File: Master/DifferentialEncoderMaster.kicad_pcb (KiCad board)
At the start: 4 copper layers, 63 x 46.5 mm, 33 parts, among them J1 RJ45_Shielded_x2, J13 ISO_GPIO, J2 CAN, J3 Conn_01x20, J4 CAN, U1 SN75C1167, U2 SN75C1167, U6 ISO7761DBQ

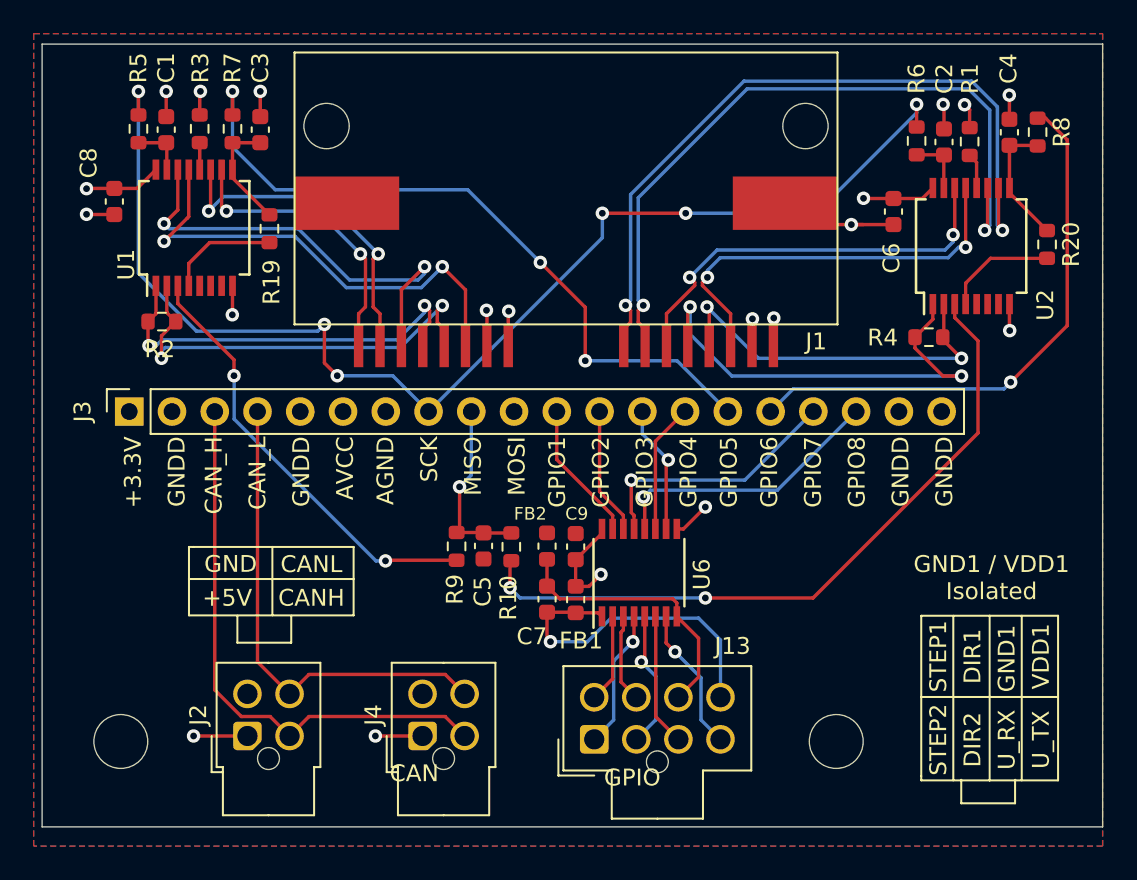
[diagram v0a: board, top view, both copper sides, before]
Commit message: Optimize layout - remove ~ 15% of vias
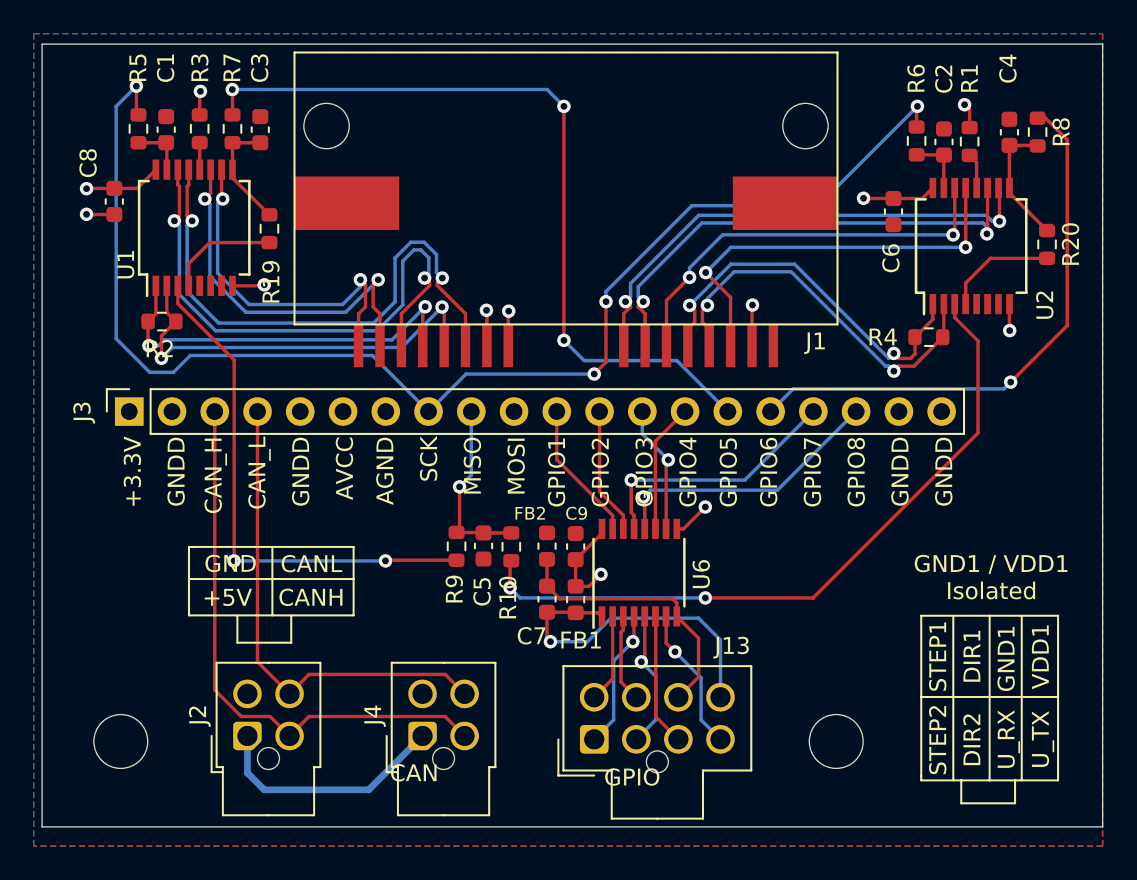
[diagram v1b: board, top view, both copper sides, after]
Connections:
- J2 pad 1: +5V -> /+12V
- J4 pad 1: +5V -> /+12V
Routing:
- net GNDD: track 25.8 -> 10.1 mm, vias 11 -> 5
- net /CSn_2+: track 44.7 -> 29.9 mm
- net /+12V: track 0.00 -> 14.3 mm
- net /CSn_2-: track 43.1 -> 29.5 mm
- net /CLK_1+: track 26.2 -> 33.3 mm
- net +5V: track 28.7 -> 22.9 mm, vias 9 -> 7
- net /SCK: track 73.5 -> 78.7 mm, vias 6 -> 4
- net /MISO_1: track 26.0 -> 31.0 mm
- net /CLK_1-: track 28.6 -> 33.3 mm
- net /GPIO5: track 42.5 -> 47.0 mm
- net /MISO_2-: track 27.6 -> 23.2 mm
- net /CSn_1+: track 16.8 -> 20.6 mm
- net /CSn_1-: track 19.5 -> 22.5 mm
- net /MISO_1+: track 25.8 -> 25.2 mm
- net /MISO_2+: track 22.5 -> 23.0 mm
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
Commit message: Further layout optimization
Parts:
- moved R10 29.5 mm to (119.1, 75.0), turned to 270 degrees
- moved R9 19.3 mm to (73.7, 74.1), turned to 270 degrees
- moved C5 19.2 mm to (75.4, 74.1), turned to 90 degrees
- moved FB2 11.7 mm to (104.1, 92.2), turned to 0 degrees
- moved C7 10.2 mm to (104.1, 90.5), turned to 180 degrees
- moved FB1 8.74 mm to (104.1, 87.1), turned to 180 degrees
- moved C9 8.46 mm to (104.1, 85.4), turned to 0 degrees
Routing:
- net /MISO: track 10.8 -> 66.1 mm, vias 1 -> 2
- net /MISO_2: track 42.0 -> 2.59 mm, vias 2 -> 0
- net /MISO_1: track 31.0 -> 3.09 mm, vias 2 -> 0
- net /GPIO5: track 47.0 -> 57.4 mm, vias 3 -> 1
- net /SCK: track 78.7 -> 88.0 mm, vias 4 -> 2
- net GND1: track 16.3 -> 7.05 mm
- net +5V: track 22.9 -> 27.7 mm
- net VDD1: track 19.8 -> 17.8 mm, vias 1 -> 0
- net GNDD: track 10.1 -> 11.7 mm, vias 5 -> 4

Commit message: Prettify CAN wires
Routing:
- net /CAN_L: track 28.9 -> 30.6 mm
- net /CAN_H: track 33.5 -> 32.5 mm
